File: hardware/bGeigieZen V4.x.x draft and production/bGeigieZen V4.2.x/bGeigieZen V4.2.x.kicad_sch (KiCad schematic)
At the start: 10 parts, among them J1 M5 2x15 pin, J3 GPS, J4 Geiger Safepulse, J5 Extra support header

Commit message: chore: update bGeigieZen V4.2.2 PCB to KiCad 10 and refine properties
Update the bGeigieZen V4.2.x PCB design to KiCad version 10.0, bumping the revision to V4.2.2. The update includes migrating the file format to the new version 20260206 standard and restructuring layer settings for tenting, covering, and plugging. Additionally, component properties have been standardized to hide names and disable autoplace, while removing obsolete HPGL plot parameters and updating the project context for better BOM and position file generation.
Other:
- title: bGeigieZen V4.2.1 -> bGeigieZen V4.2.2

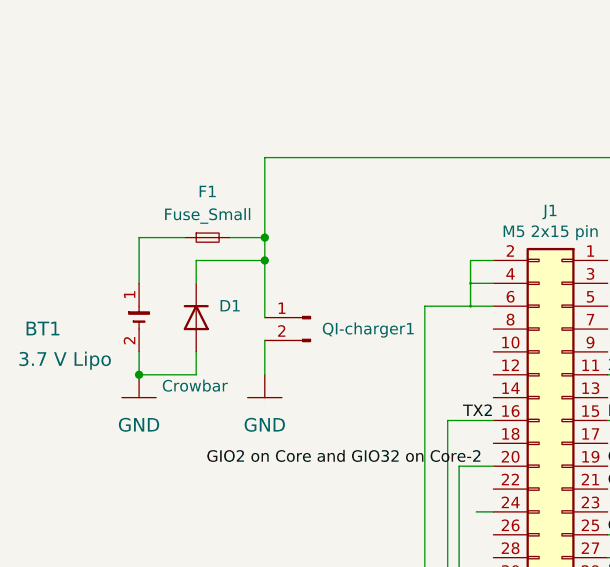
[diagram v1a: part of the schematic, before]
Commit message: chore: update bGeigieZen to V4.3.0 and add support headers
Bump hardware revision from V4.2.2 to V4.3.0 in the KiCad PCB title block.
Update the submodule reference to the latest commit.
Add new 2-pin header connectors (J4, J5) for extra support functionality.
Rename existing connector pins to avoid duplicate numbering conflicts.
Replace generic ground symbols with standard male pin headers for J4 and J5.
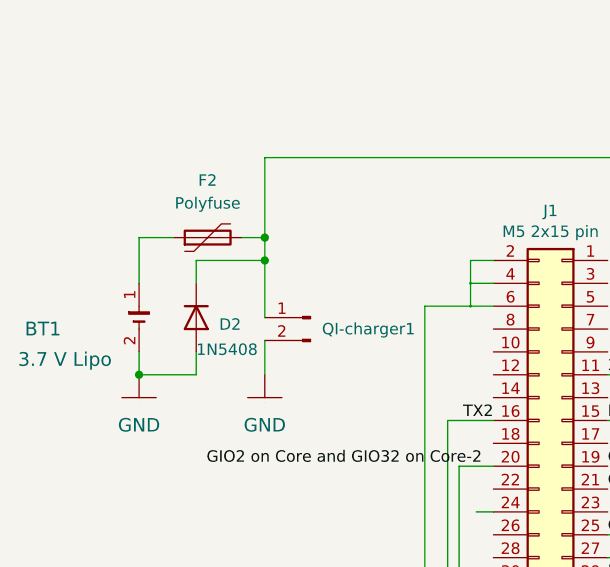
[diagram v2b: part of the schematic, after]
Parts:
- removed D1: Crowbar, Diode_THT:D_DO-201_P15.24mm_Horizontal, symbol Device:D
- removed F1: Fuse_Small, Fuse:Fuse_Littelfuse_395Series, symbol Device:Fuse_Small
- added D2: 1N5408, Diode_THT:D_DO-201AD_P15.24mm_Horizontal, symbol Diode:1N5408
- added F2: Polyfuse, Connector_PinHeader_2.54mm:PinHeader_2x01_P2.54mm_Vertical, symbol Device:Polyfuse
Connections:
- net BAT: now also D2.1 (K), F2.2
- net GND: now also D2.2 (A)
- net at BT1.1 (+): now also F2.1
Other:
- title: bGeigieZen V4.2.2 -> bGeigieZen V4.3.0
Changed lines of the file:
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@@
 	(paper "A4")
 	(title_block
-		(title "bGeigieZen V4.2.2")
+		(title "bGeigieZen V4.3.0")
 		(date "2026-03-17")
-		(rev "V4.2.2")
+		(rev "V4.3.0")
 		(company "GitHub link at https://github.com/Safecast/bGeigieZen")
 		(comment 1 "New standard version")
@@
 	(wire
 		(pts
-			(xy 93.98 73.66) (xy 99.06 73.66)
+			(xy 93.98 73.66) (xy 97.79 73.66)
 		)
 		(stroke
@@
 	(wire
 		(pts
-			(xy 104.14 73.66) (xy 107.95 73.66)
+			(xy 105.41 73.66) (xy 107.95 73.66)
 		)
 		(stroke
@@
 	)
 	(symbol
-		(lib_id "Device:Fuse_Small")
-		(at 101.6 73.66 0)
-		(unit 1)
-		(body_style 1)
-		(exclude_from_sim no)
-		(in_bom yes)
-		(on_board yes)
-		(in_pos_files yes)
-		(dnp no)
-		(fields_autoplaced yes)
-		(property "Reference" "F1"
-			(at 101.6 68.58 0)
-			(show_name no)
-			(do_not_autoplace no)
-			(effects
-				(font
-					(size 1.27 1.27)
-				)
-			)
-		)
-		(property "Value" "Fuse_Small"
-			(at 101.6 71.12 0)
-			(show_name no)
-			(do_not_autoplace no)
-			(effects
-				(font
-					(size 1.27 1.27)
-				)
-			)
-		)
-		(property "Footprint" "Fuse:Fuse_Littelfuse_395Series"
-			(at 101.6 73.66 0)
-			(hide yes)
-			(show_name no)
-			(do_not_autoplace no)
-			(effects
-				(font
-					(size 1.27 1.27)
-				)
-			)
-		)
-		(property "Datasheet" ""
-			(at 101.6 73.66 0)
-			(hide yes)
-			(show_name no)
-			(do_not_autoplace no)
-			(effects
-				(font
-					(size 1.27 1.27)
-				)
-			)
-		)
-		(property "Description" "Fuse, small symbol"
-			(at 101.6 73.66 0)
-			(hide yes)
-			(show_name no)
-			(do_not_autoplace no)
-			(effects
-				(font
-					(size 1.27 1.27)
-				)
-			)
-		)
-		(pin "2"
-		)
-		(pin "1"
-		)
-		(instances
-			(project "bGeigieZen V4.2.x"
-				(path "/c2e3a215-6a49-419d-95d1-595f35b17280"
-					(reference "F1")
-					(unit 1)
-				)
-			)
-		)
-	)
-	(symbol
 		(lib_id "Mechanical:MountingHole_Pad")
 		(at 222.885 136.525 0)
@@
 	)
 	(symbol
-		(lib_id "Device:D")
-		(at 100.33 82.55 270)
-		(unit 1)
-		(body_style 1)
-		(exclude_from_sim no)
-		(in_bom yes)
-		(on_board yes)
-		(in_pos_files yes)
-		(dnp no)
-		(property "Reference" "D1"
-			(at 102.87 81.2799 90)
-			(show_name no)
-			(do_not_autoplace no)
-			(effects
-				(font
-					(size 1.27 1.27)
-				)
-				(justify left)
-			)
-		)
-		(property "Value" "Crowbar"
-			(at 96.52 90.17 90)
-			(show_name no)
-			(do_not_autoplace no)
-			(effects
-				(font
-					(size 1.27 1.27)
-				)
-				(justify left)
-			)
-		)
-		(property "Footprint" "Diode_THT:D_DO-201_P15.24mm_Horizontal"
-			(at 100.33 82.55 0)
-			(hide yes)
-			(show_name no)
-			(do_not_autoplace no)
-			(effects
-				(font
-					(size 1.27 1.27)
-				)
-			)
-		)
-		(property "Datasheet" ""
-			(at 100.33 82.55 0)
-			(hide yes)
-			(show_name no)
-			(do_not_autoplace no)
-			(effects
-				(font
-					(size 1.27 1.27)
-				)
-			)
-		)
-		(property "Description" "Diode"
-			(at 100.33 82.55 0)
-			(hide yes)
-			(show_name no)
-			(do_not_autoplace no)
-			(effects
-				(font
-					(size 1.27 1.27)
-				)
-			)
-		)
-		(property "Sim.Device" "D"
-			(at 100.33 82.55 0)
-			(hide yes)
-			(show_name no)
-			(do_not_autoplace no)
-			(effects
-				(font
-					(size 1.27 1.27)
-				)
-			)
-		)
-		(property "Sim.Pins" "1=K 2=A"
-			(at 100.33 82.55 0)
-			(hide yes)
-			(show_name no)
-			(do_not_autoplace no)
-			(effects
-				(font
-					(size 1.27 1.27)
-				)
-			)
-		)
-		(pin "1"
-		)
-		(pin "2"
-		)
-		(instances
-			(project "bGeigieZen V4.2.x"
-				(path "/c2e3a215-6a49-419d-95d1-595f35b17280"
-					(reference "D1")
-					(unit 1)
-				)
-			)
-		)
-	)
-	(symbol
 		(lib_id "bGeigieRaku-V2-rescue:GND-bGeigieNano_V1.1.5")
 		(at 107.95 91.44 0)
@@
 					(unit 1)
 				)
+			)
+		)
+	)
+	(symbol
+		(lib_id "Diode:1N5408")
+		(at 100.33 82.55 270)
+		(unit 1)
+		(body_style 1)
+		(exclude_from_sim no)
+		(in_bom yes)
+		(on_board yes)
+		(in_pos_files yes)
+		(dnp no)
+		(property "Reference" "D2"
+			(at 102.87 83.312 90)
+			(show_name no)
+			(do_not_autoplace no)
+			(effects
+				(font
+					(size 1.27 1.27)
+				)
+				(justify left)
+			)
+		)
+		(property "Value" "1N5408"
+			(at 100.33 86.106 90)
+			(show_name no)
+			(do_not_autoplace no)
+			(effects
+				(font
+					(size 1.27 1.27)
+				)
+				(justify left)
+			)
+		)
+		(property "Footprint" "Diode_THT:D_DO-201AD_P15.24mm_Horizontal"
+			(at 95.885 82.55 0)
+			(hide yes)
+			(show_name no)
+			(do_not_autoplace no)
+			(effects
+				(font
+					(size 1.27 1.27)
+				)
+			)
+		)
+		(property "Datasheet" "http://www.vishay.com/docs/88516/1n5400.pdf"
+			(at 100.33 82.55 0)
+			(hide yes)
+			(show_name no)
+			(do_not_autoplace no)
+			(effects
+				(font
+					(size 1.27 1.27)
+				)
+			)
+		)
+		(property "Description" "1000V 3A General Purpose Rectifier Diode, DO-201AD"
+			(at 100.33 82.55 0)
+			(hide yes)
+			(show_name no)
+			(do_not_autoplace no)
+			(effects
+				(font
+					(size 1.27 1.27)
+				)
+			)
+		)
+		(property "Sim.Device" "D"
+			(at 100.33 82.55 0)
+			(hide yes)
+			(show_name no)
+			(do_not_autoplace no)
+			(effects
+				(font
+					(size 1.27 1.27)
+				)
+			)
+		)
+		(property "Sim.Pins" "1=K 2=A"
+			(at 100.33 82.55 0)
+			(hide yes)
+			(show_name no)
+			(do_not_autoplace no)
+			(effects
+				(font
+					(size 1.27 1.27)
+				)
+			)
+		)
+		(pin "1"
+		)
+		(pin "2"
+		)
+		(instances
+			(project "bGeigieZen V4.2.x"
+				(path "/c2e3a215-6a49-419d-95d1-595f35b17280"
+					(reference "D2")
+					(unit 1)
+				)
+			)
+		)
+	)
+	(symbol
+		(lib_id "Device:Polyfuse")
+		(at 101.6 73.66 90)
+		(unit 1)
+		(body_style 1)
+		(exclude_from_sim no)
+		(in_bom yes)
+		(on_board yes)
+		(in_pos_files yes)
+		(dnp no)
+		(fields_autoplaced yes)
+		(property "Reference" "F2"
+			(at 101.6 67.31 90)
+			(show_name no)
+			(do_not_autoplace no)
+			(effects
+				(font
+					(size 1.27 1.27)
+				)
+			)
+		)
+		(property "Value" "Polyfuse"
+			(at 101.6 69.85 90)
+			(show_name no)
+			(do_not_autoplace no)
+			(effects
+				(font
+					(size 1.27 1.27)
+				)
+			)
+		)
+		(property "Footprint" "Connector_PinHeader_2.54mm:PinHeader_2x01_P2.54mm_Vertical"
+			(at 106.68 72.39 0)
+			(hide yes)
+			(show_name no)
+			(do_not_autoplace no)
+			(effects
+				(font
+					(size 1.27 1.27)
+				)
+				(justify left)
+			)
+		)
+		(property "Datasheet" ""
+			(at 101.6 73.66 0)
+			(hide yes)
+			(show_name no)
+			(do_not_autoplace no)
+			(effects
+				(font
+					(size 1.27 1.27)
+				)
+			)
+		)
+		(property "Description" "Resettable fuse, polymeric positive temperature coefficient"
+			(at 101.6 73.66 0)
+			(hide yes)
+			(show_name no)
+			(do_not_autoplace no)
+			(effects
+				(font
+					(size 1.27 1.27)
+				)
+			)
+		)
+		(pin "2"
+		)
+		(pin "1"
+		)
+		(instances
+			(project "bGeigieZen V4.2.x"
+				(path "/c2e3a215-6a49-419d-95d1-595f35b17280"
+					(reference "F2")
+					(unit 1)
+				)
